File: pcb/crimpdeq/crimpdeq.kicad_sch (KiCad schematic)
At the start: 47 parts, among them J2 USB4105-GF-A, Q1 SS8550, Q2 DMG3415U, U1 ESP32-C3-MINI-1, U2 MCP73831T-2ACI/OT, U3 HX711, U4 Rust_Board, U6 SY8088

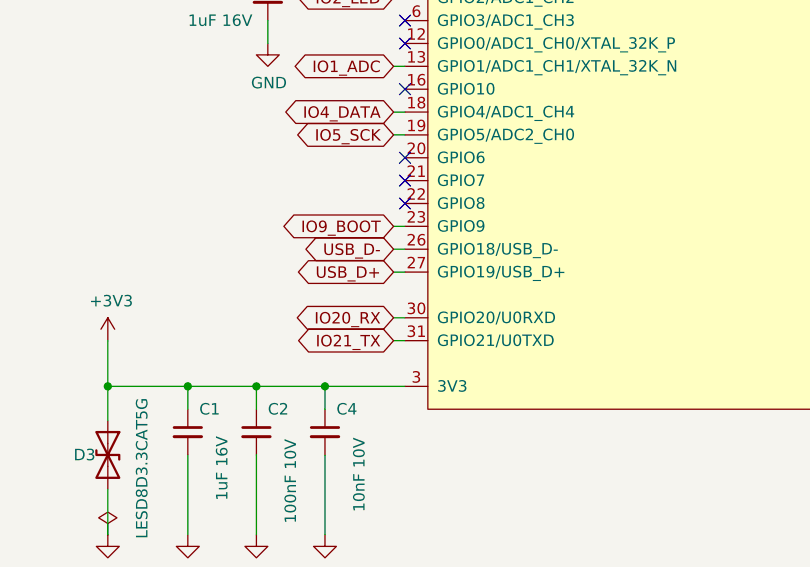
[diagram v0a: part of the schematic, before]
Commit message: fix: resolve schematic and layout rule violations
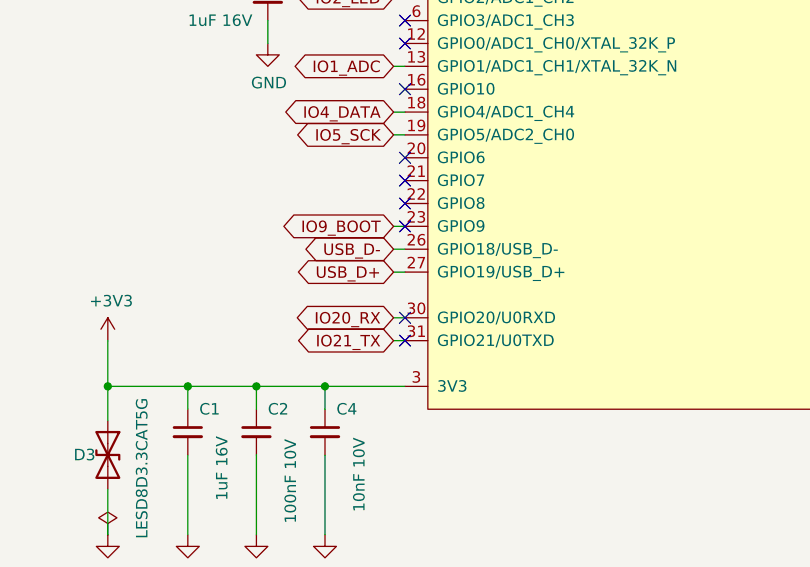
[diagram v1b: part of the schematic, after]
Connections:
- no-connect marks 10 -> 13
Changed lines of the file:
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@@
+	)
+	(no_connect
+		(at 58.42 62.23)
+	)
+	(no_connect
+		(at 58.42 72.39)
+	)
+	(no_connect
+		(at 58.42 74.93)
 	)
 	(no_connect

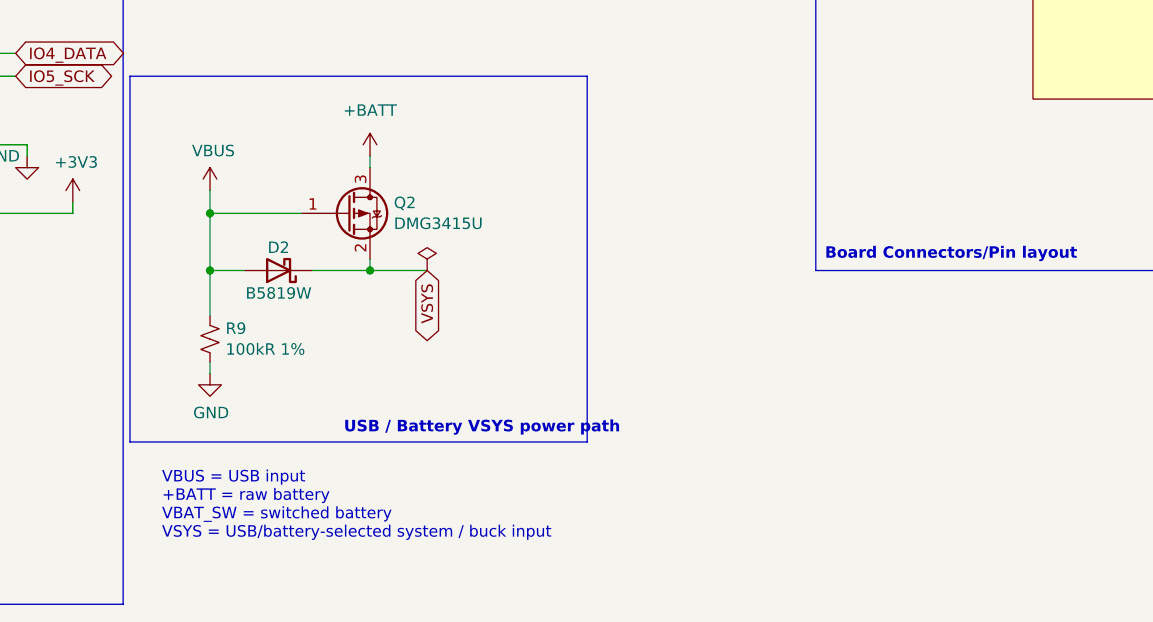
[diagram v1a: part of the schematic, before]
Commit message: fix: allow charging while switched off
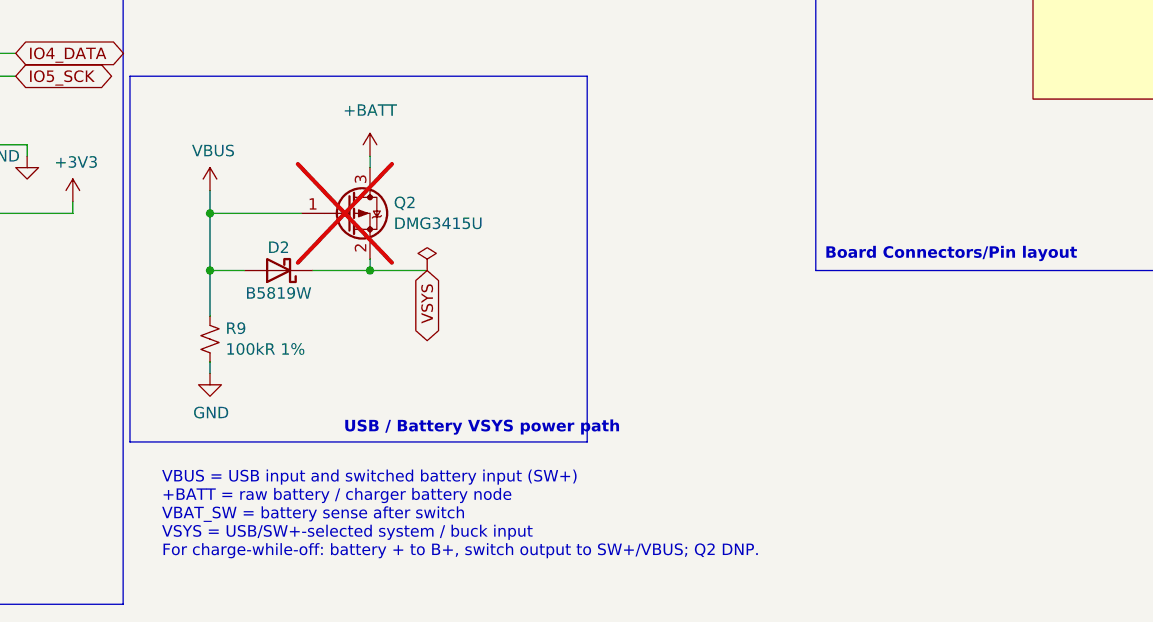
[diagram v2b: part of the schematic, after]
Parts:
- Q2: now not fitted
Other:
- note added: "VBUS = USB input and switched battery input (SW+) +BATT = raw battery / charger battery node VBAT_SW = battery sense after switch VSYS = USB/SW+-selected system / buck input For charge-while-off: battery + to B+, switch output to SW+/VBUS; Q2 DNP."
- note removed: "VBUS = USB input +BATT = raw battery VBAT_SW = switched battery VSYS = USB/battery-selected system / buck input"
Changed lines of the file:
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@@
 		)
 	)
-	(text "VBUS = USB input\n+BATT = raw battery\nVBAT_SW = switched battery\nVSYS = USB/battery-selected system / buck input"
+	(text "VBUS = USB input and switched battery input (SW+)\n+BATT = raw battery / charger battery node\nVBAT_SW = battery sense after switch\nVSYS = USB/SW+-selected system / buck input\nFor charge-while-off: battery + to B+, switch output to SW+/VBUS; Q2 DNP."
 		(exclude_from_sim no)
 		(at 125.476 182.372 0)
@@
 		(on_board yes)
 		(in_pos_files yes)
-		(dnp no)
+		(dnp yes)
 		(property "Reference" "Q2"
 			(at 151.2316 152.5016 0)
@@
 			)
 		)
-		(property "Description" ""
+		(property "Description" "DNP for charge-while-off wiring; switch output feeds SW+/VBUS pad instead."
 			(at 146.05 153.67 0)
 			(hide yes)

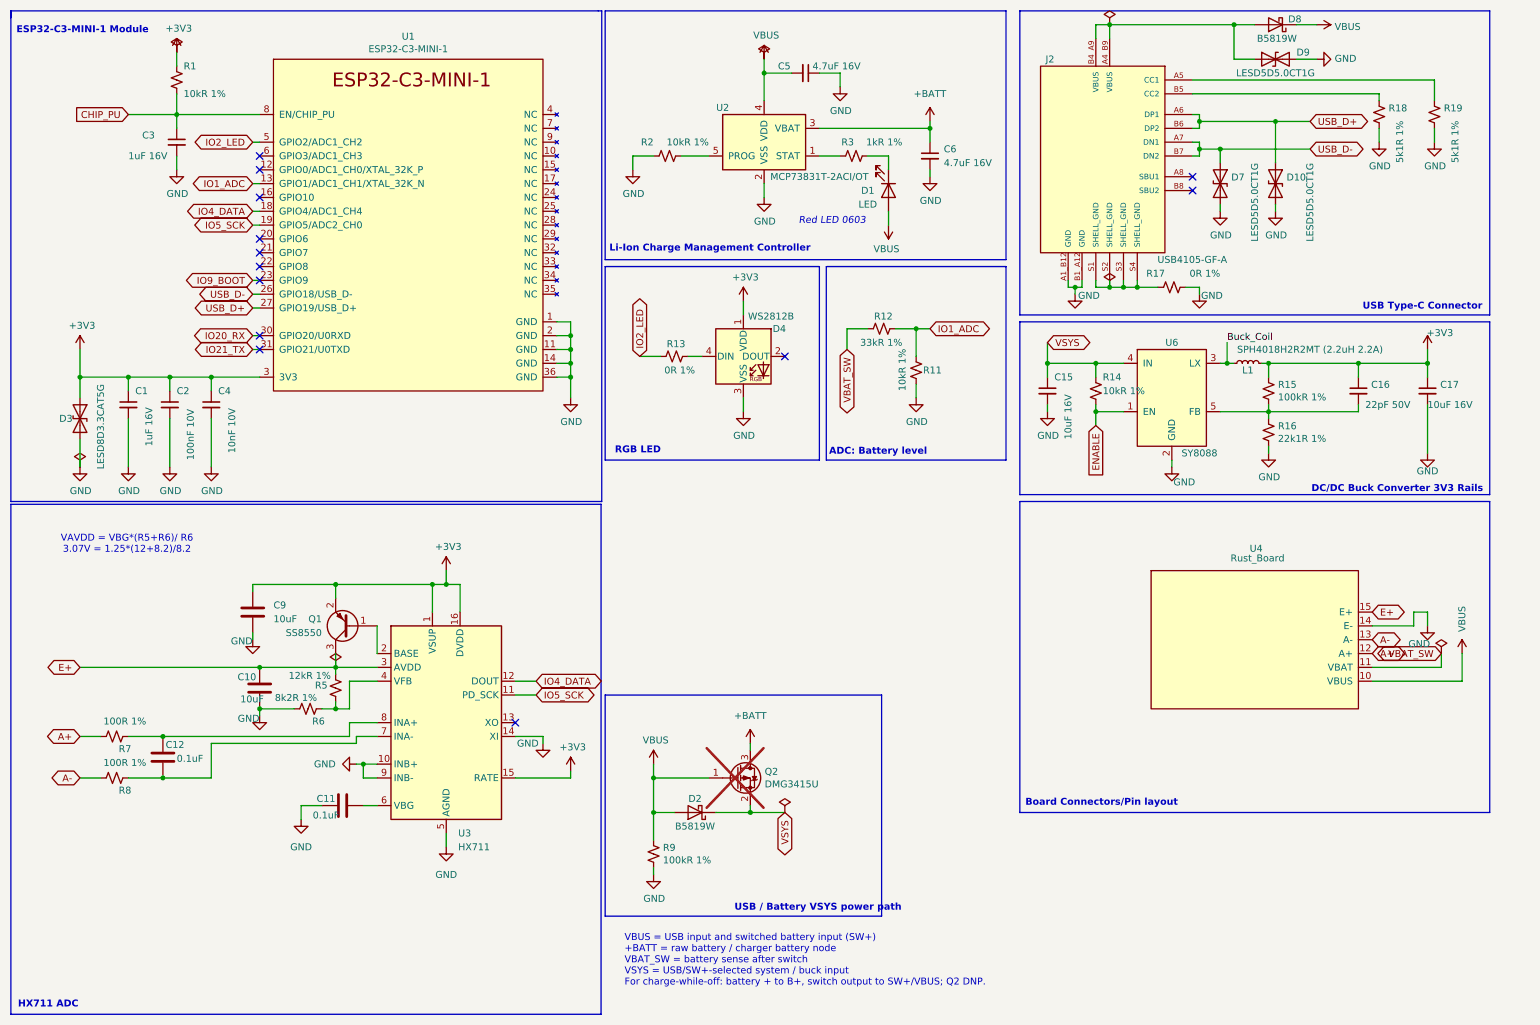
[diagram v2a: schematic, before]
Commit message: feat: Add battery gauge, review schematic/pcb
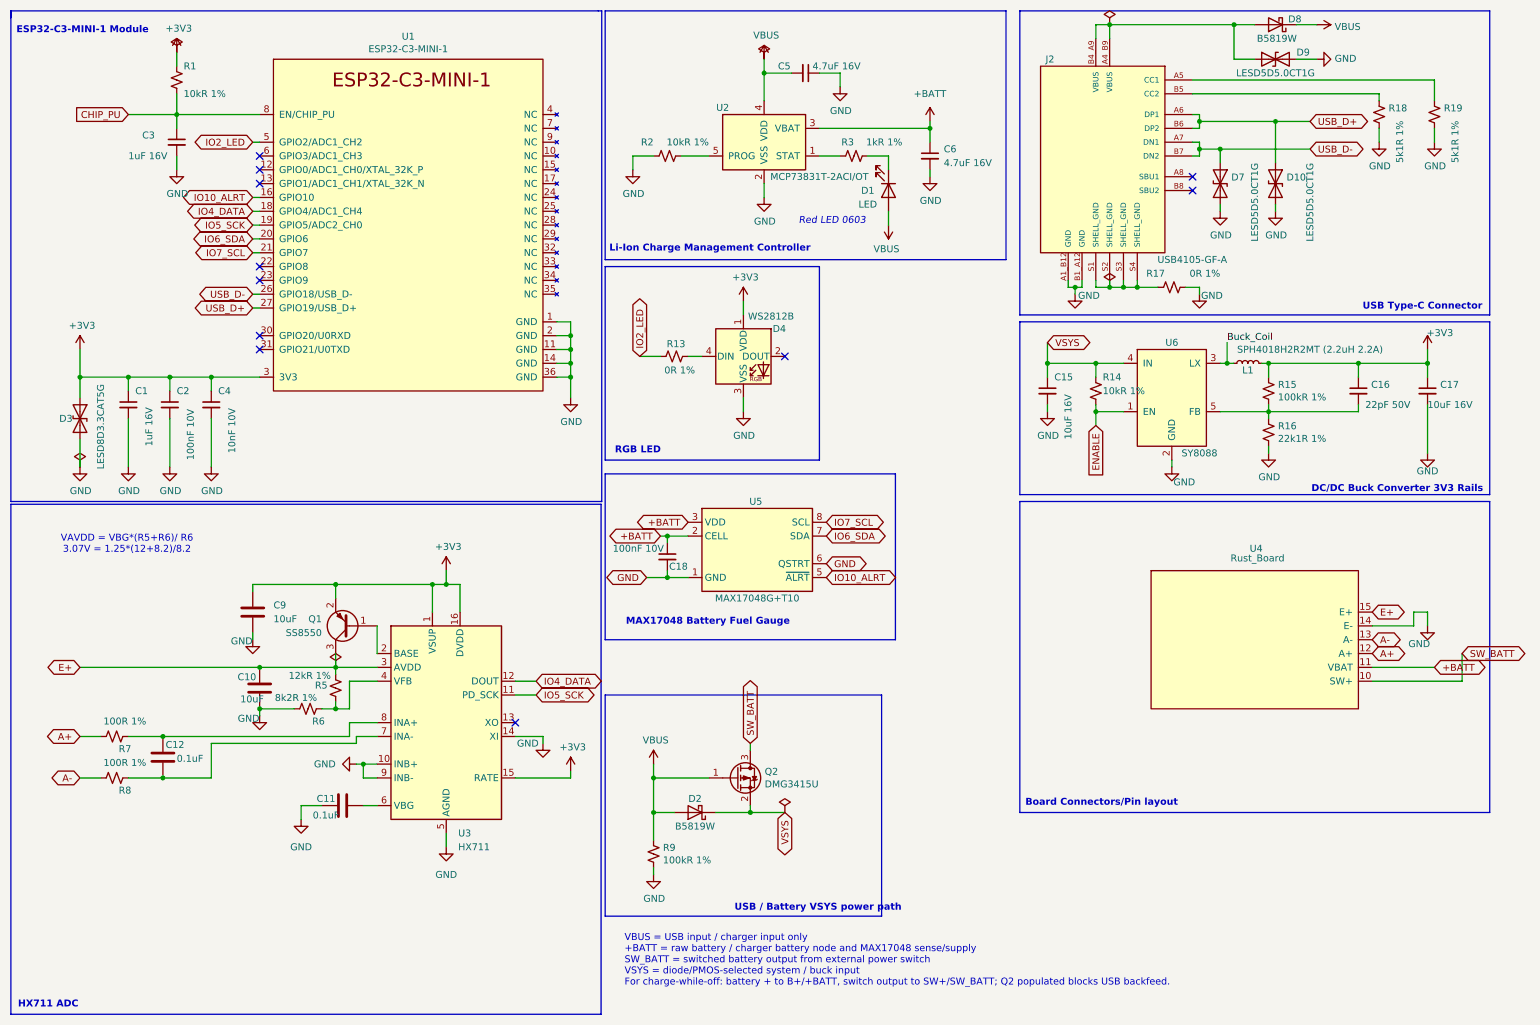
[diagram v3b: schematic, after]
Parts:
- removed R11: 10kR 1%, Resistor_SMD:R_0402_1005Metric, symbol Device:R_Small_US
- removed R12: 33kR 1%, Resistor_SMD:R_0402_1005Metric, symbol Device:R_Small_US
- added C18: 100nF 10V, Capacitor_SMD:C_0402_1005Metric, symbol Device:C_Small
- added U5: MAX17048G+T10, Package_DFN_QFN:TDFN-8-1EP_2x2mm_P0.5mm_EP0.8x1.2mm, symbol Battery_Management:MAX17048
- Q2: now fitted
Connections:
- net VBAT_SW is gone; now on net +BATT: U4.11 (VBAT)
- net +BATT: now also C18.1, U5.2 (CELL), U5.3 (VDD); no longer Q2.3 (D)
- net GND: now also C18.2, U5.1 (GND), U5.4 (GND), U5.6 (QSTRT), U5.9 (GND)
- net VBUS: no longer U4.10 (VBUS)
- net IO10_ALRT: now reaches U1.16 (GPIO10)
- net IO10_ALRT: now also U5.5 (~{ALRT})
- net IO6_SDA: now reaches U1.20 (GPIO6)
- net IO6_SDA: now also U5.7 (SDA)
- net IO7_SCL: now reaches U1.21 (GPIO7)
- net IO7_SCL: now also U5.8 (SCL)
- net IO1_ADC: no longer names the net of U1.13 (GPIO1/ADC1_CH1/XTAL_32K_N)
- net IO20_RX: no longer names the net of U1.30 (GPIO20/U0RXD)
- net IO21_TX: no longer names the net of U1.31 (GPIO21/U0TXD)
- net IO9_BOOT: no longer names the net of U1.23 (GPIO9)
- new net SW_BATT: Q2.3 (D), U4.10 (SW+)
- no-connect marks 13 -> 11
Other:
- note added: "MAX17048 Battery Fuel Gauge"
- note added: "VBUS = USB input / charger input only +BATT = raw battery / charger battery node and MAX17048 sense/supply SW_BATT = switched battery output from external power switch VSYS = diode/PMOS-selected system / buck input For charge-while-off: battery + to B+/+BATT, switch output to SW+/SW_BATT; Q2 populated blocks USB backfeed."
- note removed: "ADC: Battery level"
- note removed: "VBUS = USB input and switched battery input (SW+) +BATT = raw battery / charger battery node VBAT_SW = battery sense after switch VSYS = USB/SW+-selected system / buck input For charge-while-off: battery + to B+, switch output to SW+/VBUS; Q2 DNP."

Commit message: feat: Update Assembly note of R13
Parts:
- R13: AssemblyNote Critical value: 33kΩ 0402 resistor. Do not use 10kΩ. -> (none)
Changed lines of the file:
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@@
 		(at 58.42 39.37)
 	)
-	(wire
-		(pts
-			(xy 262.89 133.35) (xy 274.32 133.35)
-		)
-		(stroke
-			(width 0)
-			(type default)
-		)
-	)
-	(global_label "+BATT"
-		(shape bidirectional)
-		(at 274.32 133.35 0)
-		(fields_autoplaced yes)
-		(effects
-			(font
-				(size 1.27 1.27)
-			)
-			(justify left)
-		)
-		(property "Intersheetrefs" "${INTERSHEET_REFS}"
-			(at 281.9073 133.35 0)
-			(hide yes)
-			(show_name no)
-			(do_not_autoplace no)
-			(effects
-				(font
-					(size 1.27 1.27)
-				)
-				(justify left)
-			)
-		)
-	)
 	(no_connect
 		(at 58.42 72.39)
@@
 	(wire
 		(pts
+			(xy 262.89 133.35) (xy 274.32 133.35)
+		)
+		(stroke
+			(width 0)
+			(type default)
+		)
+	)
+	(wire
+		(pts
 			(xy 262.89 135.89) (xy 279.4 135.89)
 		)
@@
 		)
 	)
+	(global_label "SW_BATT"
+		(shape bidirectional)
+		(at 148.59 147.32 90)
+		(fields_autoplaced yes)
+		(effects
+			(font
+				(size 1.27 1.27)
+			)
+			(justify left)
+		)
+		(property "Intersheetrefs" "${INTERSHEET_REFS}"
+			(at 148.59 140.1853 90)
+			(hide yes)
+			(show_name no)
+			(do_not_autoplace no)
+			(effects
+				(font
+					(size 1.27 1.27)
+				)
+				(justify left)
+			)
+		)
+	)
 	(global_label "ENABLE"
 		(shape input)
@@
 		)
 	)
+	(global_label "SW_BATT"
+		(shape bidirectional)
+		(at 279.4 130.81 0)
+		(fields_autoplaced yes)
+		(effects
+			(font
+				(size 1.27 1.27)
+			)
+			(justify left)
+		)
+		(property "Intersheetrefs" "${INTERSHEET_REFS}"
+			(at 288.5675 130.81 0)
+			(hide yes)
+			(show_name no)
+			(do_not_autoplace no)
+			(effects
+				(font
+					(size 1.27 1.27)
+				)
+				(justify left)
+			)
+		)
+	)
 	(global_label "IO4_DATA"
 		(shape bidirectional)
@@
 		)
 	)
-	(global_label "A-"
+	(global_label "+BATT"
 		(shape bidirectional)
-		(at 25.4 153.67 180)
+		(at 274.32 133.35 0)
 		(fields_autoplaced yes)
 		(effects
@@
 				(size 1.27 1.27)
 			)
-			(justify right)
+			(justify left)
 		)
 		(property "Intersheetrefs" "${INTERSHEET_REFS}"
-			(at 18.6425 153.67 0)
+			(at 281.9073 133.35 0)
 			(hide yes)
 			(show_name no)
@@
 					(size 1.27 1.27)
 				)
-				(justify right)
+				(justify left)
 			)
 		)
 	)
-	(global_label "USB_D-"
+	(global_label "A-"
 		(shape bidirectional)
-		(at 251.46 38.1 0)
+		(at 25.4 153.67 180)
 		(fields_autoplaced yes)
 		(effects
@@
 				(size 1.27 1.27)
 			)
-			(justify left)
+			(justify right)
 		)
 		(property "Intersheetrefs" "${INTERSHEET_REFS}"
-			(at 262.3635 38.1 0)
+			(at 18.6425 153.67 0)
 			(hide yes)
 			(show_name no)
@@
 					(size 1.27 1.27)
 				)
-				(justify left)
+				(justify right)
 			)
 		)
 	)
-	(global_label "USB_D+"
+	(global_label "USB_D-"
 		(shape bidirectional)
-		(at 57.15 67.31 180)
+		(at 251.46 38.1 0)
 		(fields_autoplaced yes)
 		(effects
@@
 				(size 1.27 1.27)
 			)
-			(justify right)
+			(justify left)
 		)
 		(property "Intersheetrefs" "${INTERSHEET_REFS}"
-			(at 46.2465 67.31 0)
+			(at 262.3635 38.1 0)
 			(hide yes)
 			(show_name no)
@@
 					(size 1.27 1.27)
 				)
-				(justify right)
+				(justify left)
 			)
 		)
 	)
-	(global_label "E+"
+	(global_label "USB_D+"
 		(shape bidirectional)
-		(at 262.89 123.19 0)
+		(at 57.15 67.31 180)
 		(fields_autoplaced yes)
 		(effects
@@
 				(size 1.27 1.27)
 			)
-			(justify left)
+			(justify right)
 		)
 		(property "Intersheetrefs" "${INTERSHEET_REFS}"
-			(at 269.7079 123.19 0)
+			(at 46.2465 67.31 0)
 			(hide yes)
 			(show_name no)
@@
 					(size 1.27 1.27)
 				)
-				(justify left)
+				(justify right)
 			)
 		)
 	)
-	(global_label "SW_BATT"
+	(global_label "E+"
 		(shape bidirectional)
-		(at 148.59 147.32 90)
+		(at 262.89 123.19 0)
 		(fields_autoplaced yes)
 		(effects
@@
 		)
 		(property "Intersheetrefs" "${INTERSHEET_REFS}"
-			(at 148.59 140.1853 90)
+			(at 269.7079 123.19 0)
 			(hide yes)
 			(show_name no)
@@
 		)
 	)
-	(global_label "SW_BATT"
-		(shape bidirectional)
-		(at 279.4 130.81 0)
-		(fields_autoplaced yes)
-		(effects
-			(font
-				(size 1.27 1.27)
-			)
-			(justify left)
-		)
-		(property "Intersheetrefs" "${INTERSHEET_REFS}"
-			(at 288.5675 130.81 0)
-			(hide yes)
-			(show_name no)
-			(do_not_autoplace no)
-			(effects
-				(font
-					(size 1.27 1.27)
-				)
-				(justify left)
-			)
-		)
-	)
 	(symbol
 		(lib_id "power:+3V3")
@@
 			)
 		)
-		(property "AssemblyNote" "Critical value: 33kΩ 0402 resistor. Do not use 10kΩ."
+		(property "AssemblyNote" ""
 			(at 134.62 76.2 0)
 			(hide yes)
